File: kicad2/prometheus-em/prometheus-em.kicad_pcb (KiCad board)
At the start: 2 copper layers, 42 x 40 mm, 93 parts, among them IC1 RP2040, IC10 NJM2878F3-33-TE2, IC11 S-24CM01CI-J8T1U4, IC2 SIT2001BI-S2-33E-12.000000G, IC3 W25Q128JVSIQ, IC4 TB67H450FNG,EL, IC5 TB67H450FNG,EL, IC6 PCA9306DCUR, IC7 S-89431ACMC-HBVT2U, IC8 NJM2884U1-33-TE1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

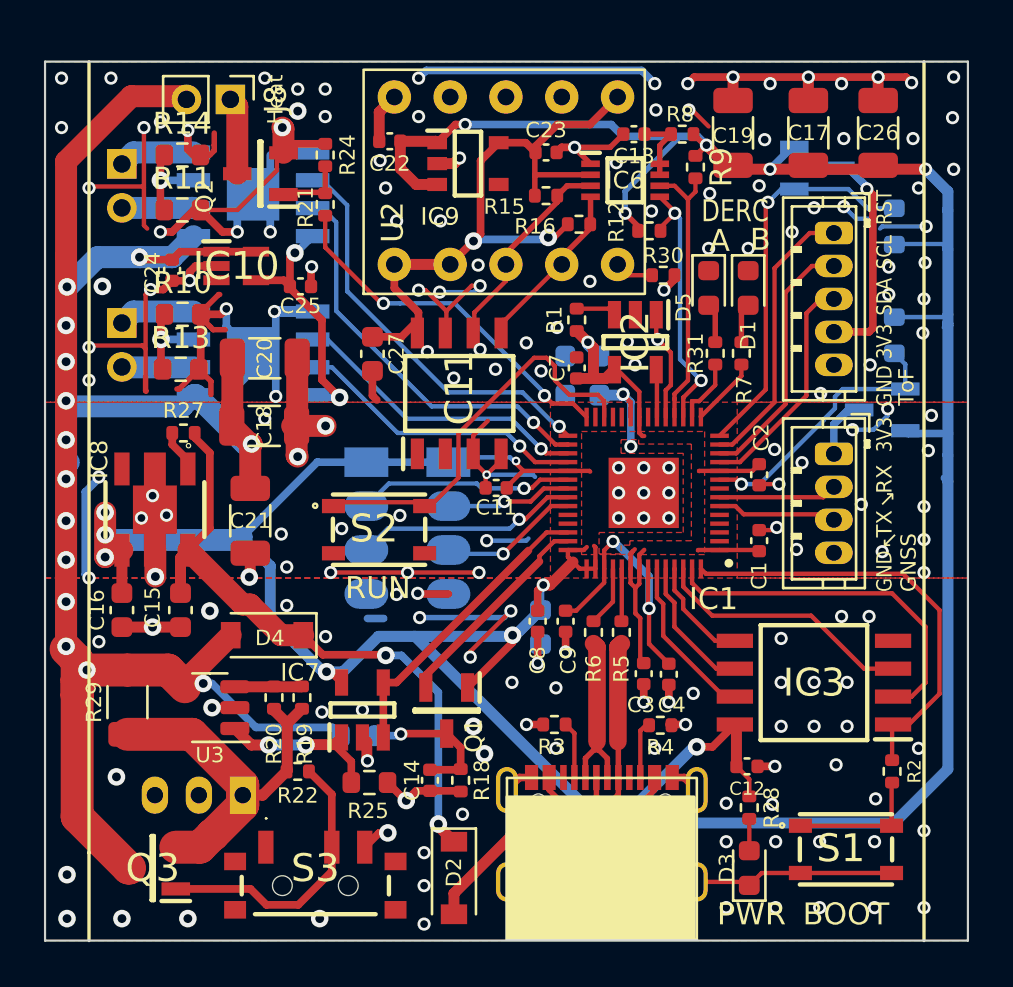
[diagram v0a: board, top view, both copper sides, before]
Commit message: add ir feature
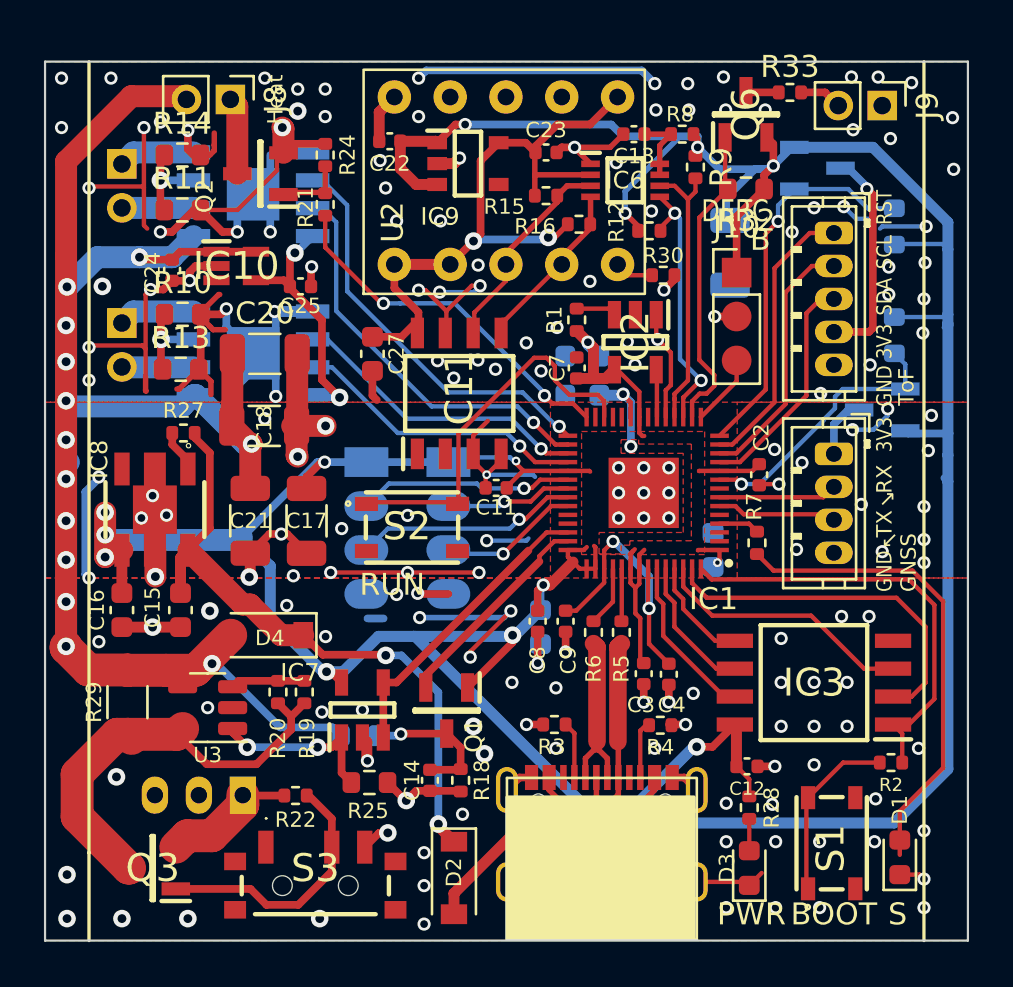
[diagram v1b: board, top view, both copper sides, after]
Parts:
- removed C26: 100u, Capacitor_SMD:C_1206_3216Metric
- removed D5: LED, LED_SMD:LED_0603_1608Metric
- removed R31: 1k, Resistor_SMD:R_0402_1005Metric
- added J10: IR_IN, Connector_PinHeader_2.00mm:PinHeader_1x03_P2.00mm_Vertical, F.Cu at (67.5, 45.6)
- added J9: IR_LED, Connector_PinHeader_2.00mm:PinHeader_1x02_P2.00mm_Vertical, F.Cu at (74.1, 38.0)
- added Q6: IRLML6402, SamacSys_Parts:SOT95P237X112-3N, F.Cu at (67.9, 38.4)
- added R32: 30k, Resistor_SMD:R_0603_1608Metric, F.Cu at (67.9, 41.8)
- added R33: 50, Resistor_SMD:R_0402_1005Metric, F.Cu at (69.9, 37.4)
- C1: footprint Capacitor_SMD:C_0402_1005Metric -> Capacitor_SMD:C_0603_1608Metric; moved to B.Cu
- C19: moved to B.Cu
- moved C17 28.9 mm to (47.9, 56.9), turned to -90 degrees
- moved D1 26.8 mm to (74.9, 72.2), turned to 90 degrees
- moved R7 8.65 mm to (68.4, 57.9), turned to -90 degrees
- moved C19 5.46 mm to (67.2, 44.7), turned to -90 degrees
- moved C1 2.14 mm to (66.4, 58.2)
- moved S2 1.50 mm to (52.7, 57.2)
- moved R22 1.10 mm to (47.4, 69.4)
- moved S1 0.71 mm to (71.8, 71.6), turned to 90 degrees
- moved R2 0.40 mm to (74.5, 67.9), turned to 0 degrees
- moved R20 0.31 mm to (46.6, 64.7)
- moved R19 0.28 mm to (47.8, 64.7)
- moved C20 0.20 mm to (46.0, 49.3)
- moved U3 0.10 mm to (43.4, 65.4)
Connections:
- IC1 pad 15: /GPIO12_LED -> /GPIO12_IR_IN
- IC1 pad 16: /GPIO13_LED -> /GPIO12_IR_OUT
- IC1 pad 4: unconnected-(IC1-Pad4) -> /GPIO2_LED
- IC1 pad 5: unconnected-(IC1-Pad5) -> /GPIO3_LED
- J7 pad 1: /BAT_IN -> Net-(J7-Pad1)
- Q3 pad 2: /BAT_IN -> Net-(J7-Pad1)
- Q3 pad 3: /7V4 -> /BAT_IN
- R22 pad 1: /BAT_IN -> Net-(J7-Pad1)
- R7 pad 1: /GPIO12_LED -> /GPIO2_LED
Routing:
- net Net-(D1-Pad2): track 1.81 -> 21.5 mm
- net GND: track 184.6 -> 167.6 mm, vias 198 -> 191
- net /7V4: track 105.7 -> 90.7 mm, vias 14 -> 13
- net /GPIO12_IR_OUT: track 0.00 -> 14.2 mm
- net +3V3: track 197.3 -> 205.9 mm, vias 14 -> 15
- net Net-(J7-Pad1): track 0.00 -> 6.19 mm
- net /GPIO12_IR_IN: track 0.00 -> 3.27 mm
- net /GPIO12_LED: track 3.15 -> 0.00 mm
- net /GPIO13_LED: track 3.01 -> 0.00 mm
- net /BAT_IN: track 17.4 -> 19.9 mm
- net Net-(R2-Pad1): track 6.13 -> 8.14 mm
- net Net-(J9-Pad2): track 0.00 -> 1.94 mm
- net Net-(D5-Pad2): track 1.87 -> 0.00 mm
- net /GPIO2_LED: track 0.00 -> 1.85 mm
- net Net-(Q6-Pad3): track 0.00 -> 1.51 mm
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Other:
- board text added: "S"
- board text removed: "A"
